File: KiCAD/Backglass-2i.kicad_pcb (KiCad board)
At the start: 2 copper layers, 48.3 x 40.6 mm, 53 parts, among them J1 IO Header, J11 Header_ICSP_AVR, J12 Header_ICSP_AVR, J13 Header_ICSP_AVR, J2 RAMP Header, J3 LOSE Header, J4 Micro_USB_Connector, J5 Batteries, Q1 MOSFET_N_E_Dual, Q2 MOSFET_N_E_Dual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

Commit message: Minor versioning updates
Changed Git.io link on silkscreen, updated version of schematic to 2.1, made note of changing I/O section.
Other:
- board text added: "git.io/fj45f"
- board text removed: "git.io/v9lfx"
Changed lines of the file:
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@@
-(kicad_pcb (version 4) (host pcbnew 4.0.3-stable)
+(kicad_pcb (version 4) (host pcbnew 4.0.7)
   (general
     (links 175)
@@
   )
   (setup
-    (last_trace_width 0.6)
+    (last_trace_width 0.25)
     (user_trace_width 0.2)
     (user_trace_width 0.4)
@@
     (effects (font (size 1 1) (thickness 0.2)) (justify mirror))
   )
-  (gr_text git.io/v9lfx (at 163.77 93.55 90) (layer B.SilkS)
+  (gr_text git.io/fj45f (at 163.77 93.55 90) (layer B.SilkS)
     (effects (font (size 1 1) (thickness 0.2)) (justify mirror))
   )
@@
   (segment (start 123.39 108.19) (end 124.41 107.17) (width 0.25) (layer B.Cu) (net 3))
   (segment (start 121.16 108.19) (end 122.66 108.19) (width 0.25) (layer B.Cu) (net 3))
-  (segment (start 157.19 104.17) (end 157.19 103.29) (width 0.6) (layer B.Cu) (net 4) (status 400000))
+  (segment (start 157.19 104.17) (end 157.19 103.29) (width 0.6) (layer B.Cu) (net 4))
   (segment (start 153.69 104.18) (end 154.85 103.02) (width 0.6) (layer B.Cu) (net 4))
   (segment (start 153.69 104.18) (end 153.69 104.98) (width 0.6) (layer B.Cu) (net 4))

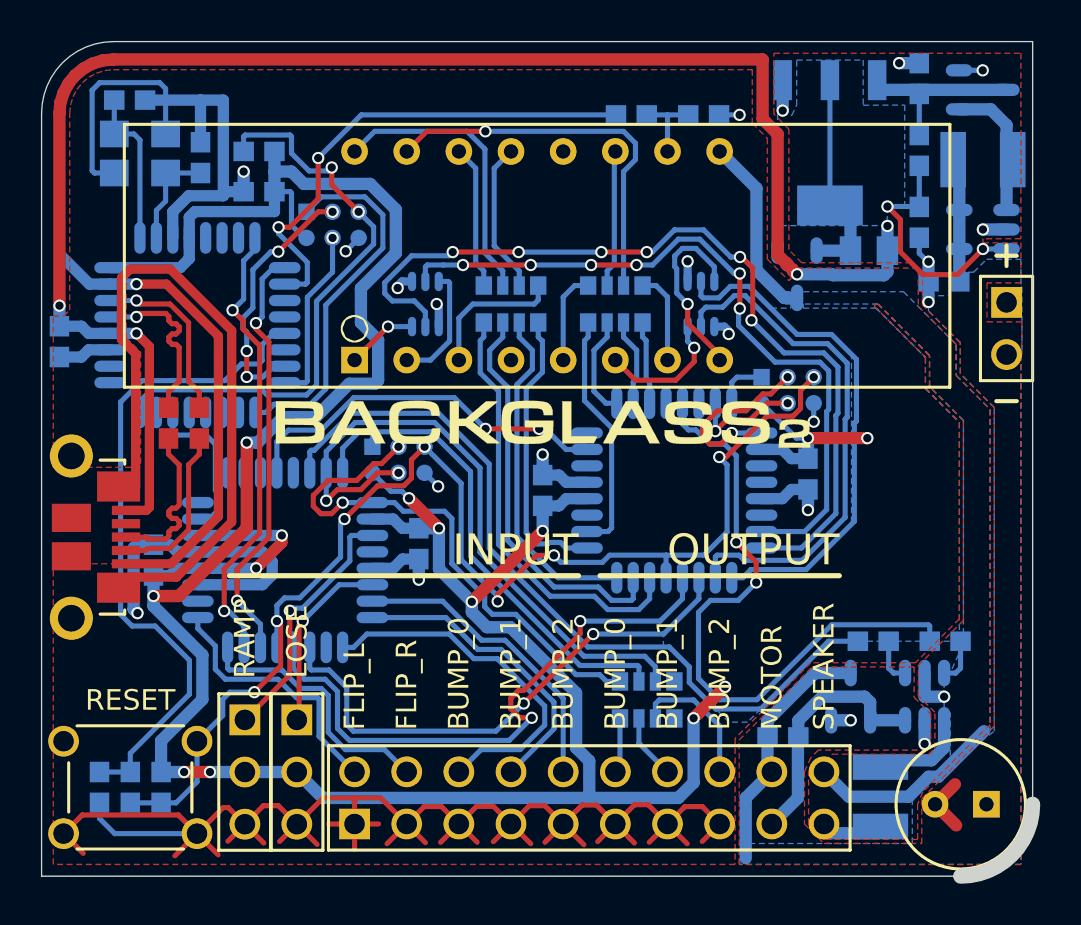
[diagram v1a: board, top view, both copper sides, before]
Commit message: Updated layout
Changed I/O connector and rerouted traces, removed I/O labels, updated logo
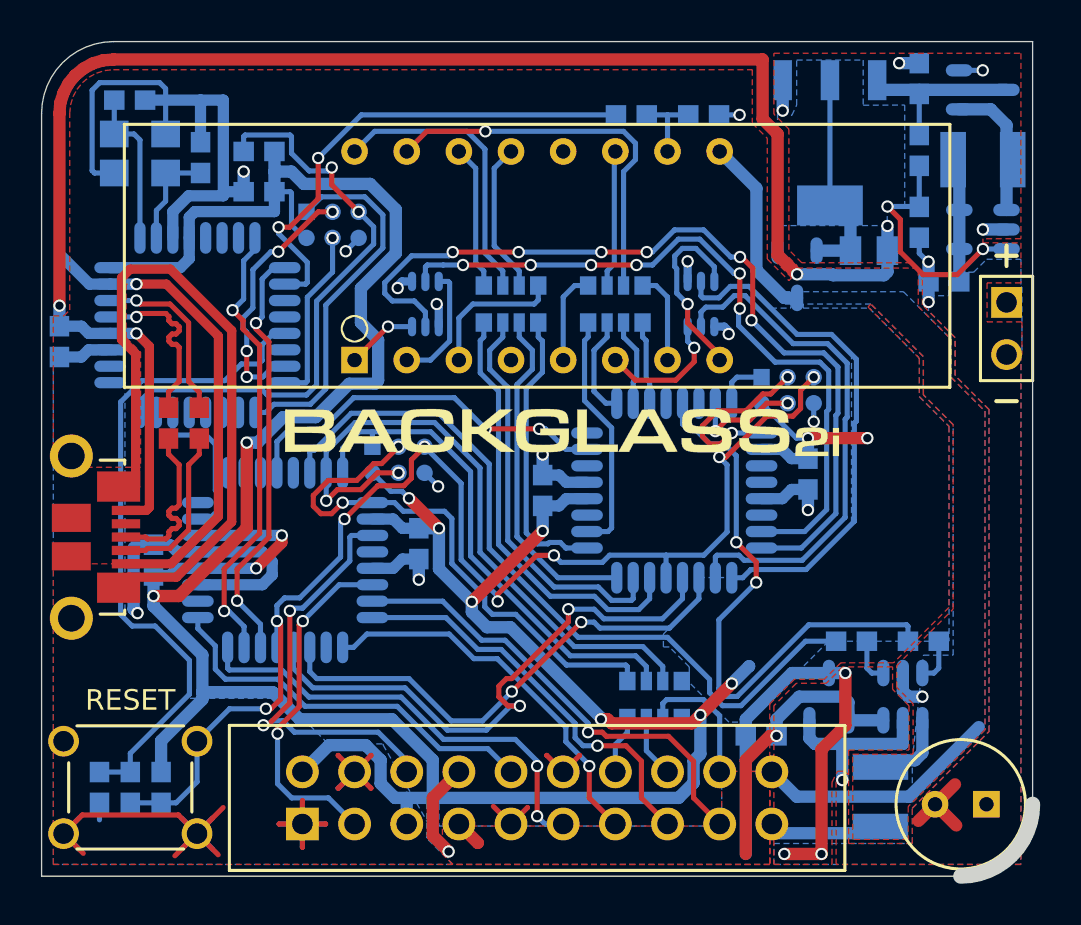
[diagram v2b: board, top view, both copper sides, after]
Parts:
- removed the G*** at (141.3, 89.8)
- removed the J2 at (126.7, 106.7)
- removed the J3 at (129.3, 106.7)
- added G***: LOGO, temp:logo, F.Cu at (142.2, 90.1)
- J1: value IO Header -> IO_Header; footprint I_Through-hole:10x2_0.1in -> X_Proprietary:TE_1-746610-5
- moved J1 2.54 mm to (141.0, 108.0)
- moved C3 1.06 mm to (151.9, 104.9)
- moved D1 1.06 mm to (155.2, 103.0)
- moved Q1 1.06 mm to (158.8, 103.0)
- moved R8 1.06 mm to (156.3, 100.3)
- moved R9 1.06 mm to (159.8, 100.3)
- moved RN3 0.36 mm to (146.7, 103.2)
- renumbered J4 to J2, J5 to J3
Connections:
- D2 pad : GND -> (no net)
- J1 pad 10: BUMP_2_SENSE -> FLIP_L_SENSE
- J1 pad 11: GND -> FLIP_R_SENSE
- J1 pad 12: BUMP_0_LED -> GND
- J1 pad 13: GND -> BUMP_0_SENSE
- J1 pad 14: BUMP_1_LED -> BUMP_0_LED
- J1 pad 15: GND -> BUMP_1_SENSE
- J1 pad 16: BUMP_2_LED -> BUMP_1_LED
- J1 pad 17: MOTOR- -> BUMP_2_SENSE
- J1 pad 18: +V_BATT -> BUMP_2_LED
- J1 pad 2: FLIP_L_SENSE -> +5V
- J1 pad 3: GND -> LOSE_SENSE
- J1 pad 4: FLIP_R_SENSE -> GND
- J1 pad 5: GND -> +5V
- J1 pad 6: BUMP_0_SENSE -> RAMP_SENSE
- J1 pad 7: GND -> MOTOR-
- J1 pad 8: BUMP_1_SENSE -> +V_BATT
- X1 pad : GND -> (no net)
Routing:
- net GND: track 230.0 -> 198.4 mm, vias 26 -> 24
- net +5V: track 166.2 -> 182.2 mm, vias 14 -> 13
- net +V_BATT: track 18.6 -> 34.4 mm, vias 0 -> 4
- net FLIP_R_SENSE: track 12.9 -> 22.1 mm, vias 0 -> 2
- net RAMP_SENSE: track 12.4 -> 20.9 mm, vias 1 -> 2
- net LOSE_SENSE: track 9.05 -> 17.1 mm, vias 1 -> 2
- net BUMP_2_SENSE: track 14.8 -> 22.7 mm, vias 0 -> 1
- net FLIP_L_SENSE: track 12.8 -> 19.3 mm
- net BUMP_1_SENSE: track 14.8 -> 20.0 mm, vias 0 -> 1
- net AUDIO_SIG: track 31.4 -> 28.3 mm
- net MOTOR-: track 12.6 -> 15.3 mm, vias 0 -> 1
- net SPEAKER-: track 3.33 -> 5.87 mm
- net MOTOR_SIG: track 38.7 -> 37.4 mm
- net (no net): track 34.2 -> 35.4 mm, vias 0 -> 1
- net SDA: track 26.0 -> 24.8 mm
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- added copper zone on F.Cu, net +V_BATT
- added copper zone on B.Cu, net GND
- added copper zone on F.Cu, net MOTOR-
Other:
- board text added: "rev2.1"
- board text removed: "BUMP_0"
- board text removed: "BUMP_1"
- board text removed: "BUMP_2"
- board text removed: "FLIP_L"
- board text removed: "FLIP_R"
- board text removed: "INPUT"
- board text removed: "LOSE"
- board text removed: "MOTOR"
- board text removed: "OUTPUT"
- board text removed: "RAMP"
- board text removed: "SPEAKER"
- board text removed: "rev2"
